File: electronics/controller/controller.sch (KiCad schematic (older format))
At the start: 17 parts

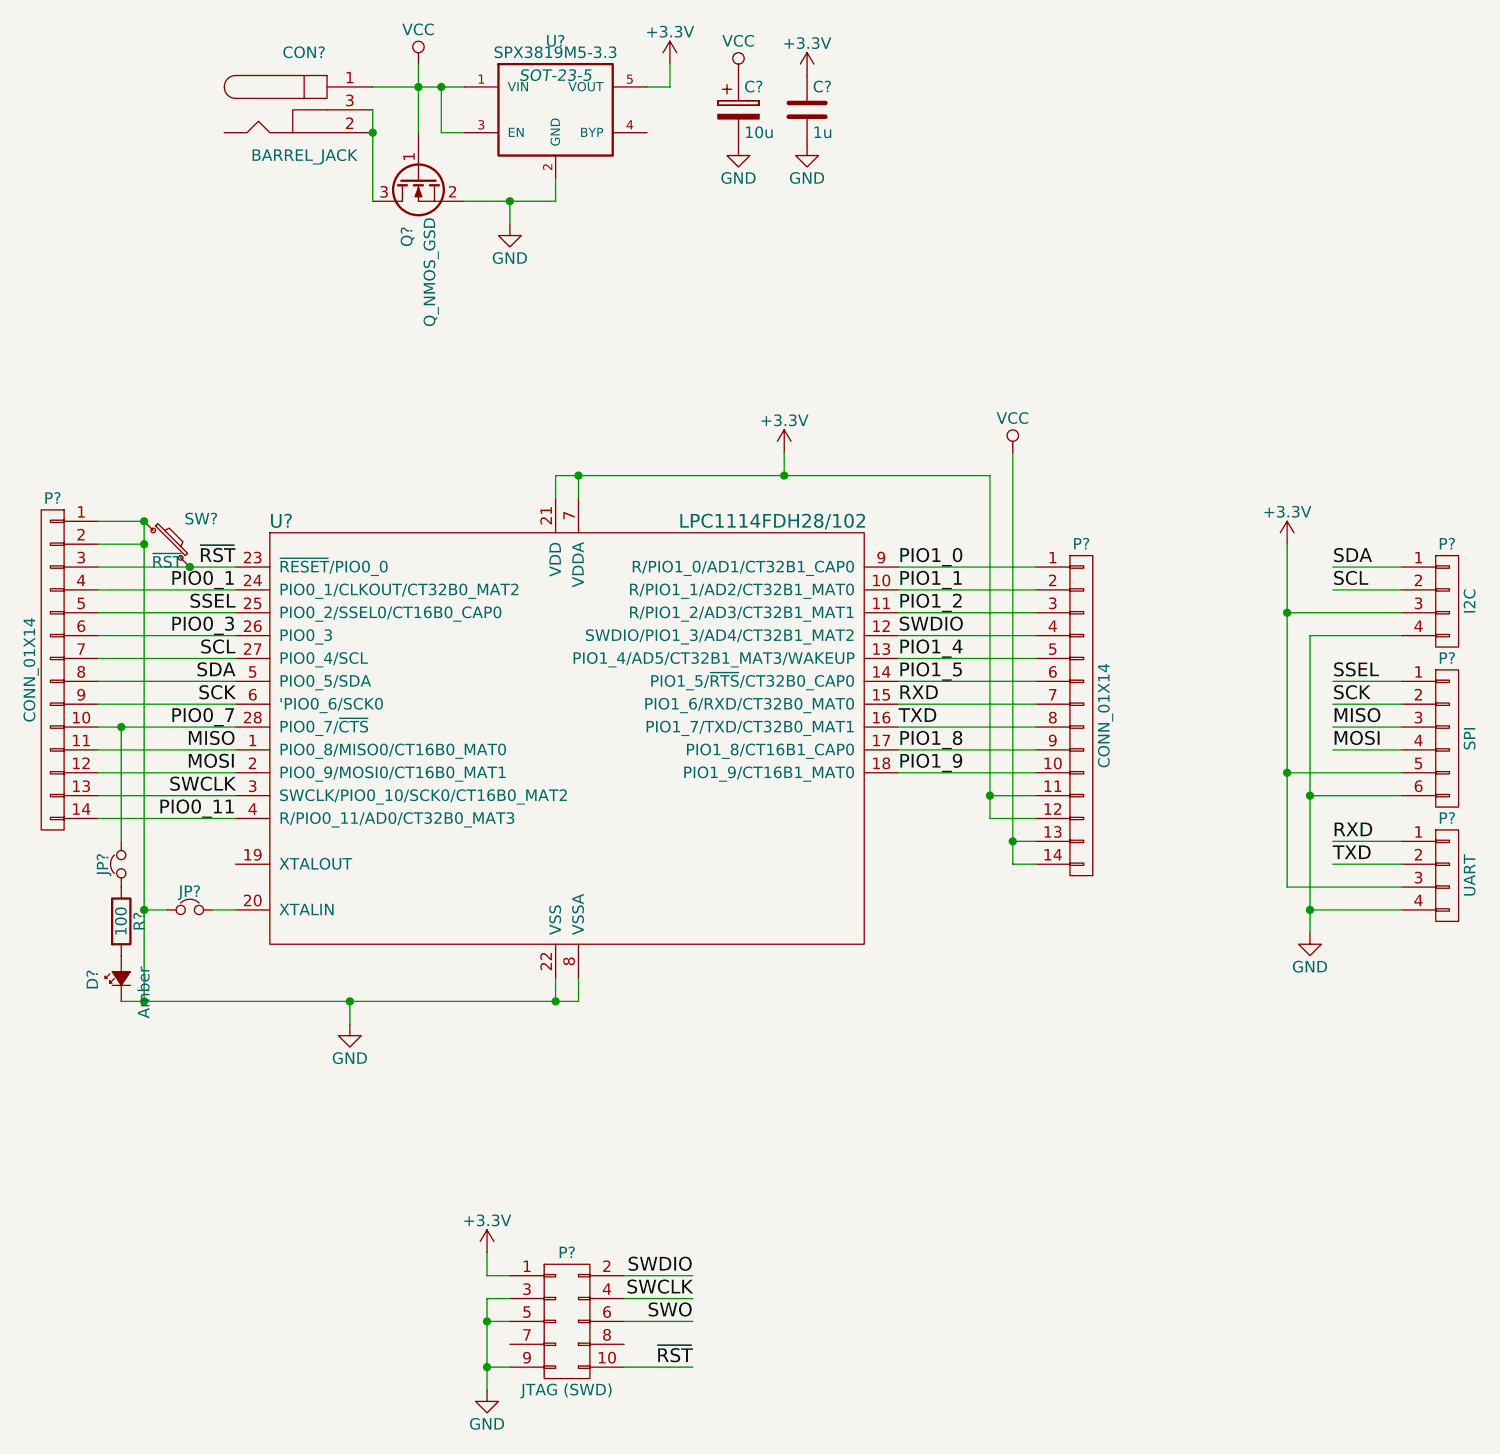
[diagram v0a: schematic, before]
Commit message: Switch to LP2985 regulator, begin board layout
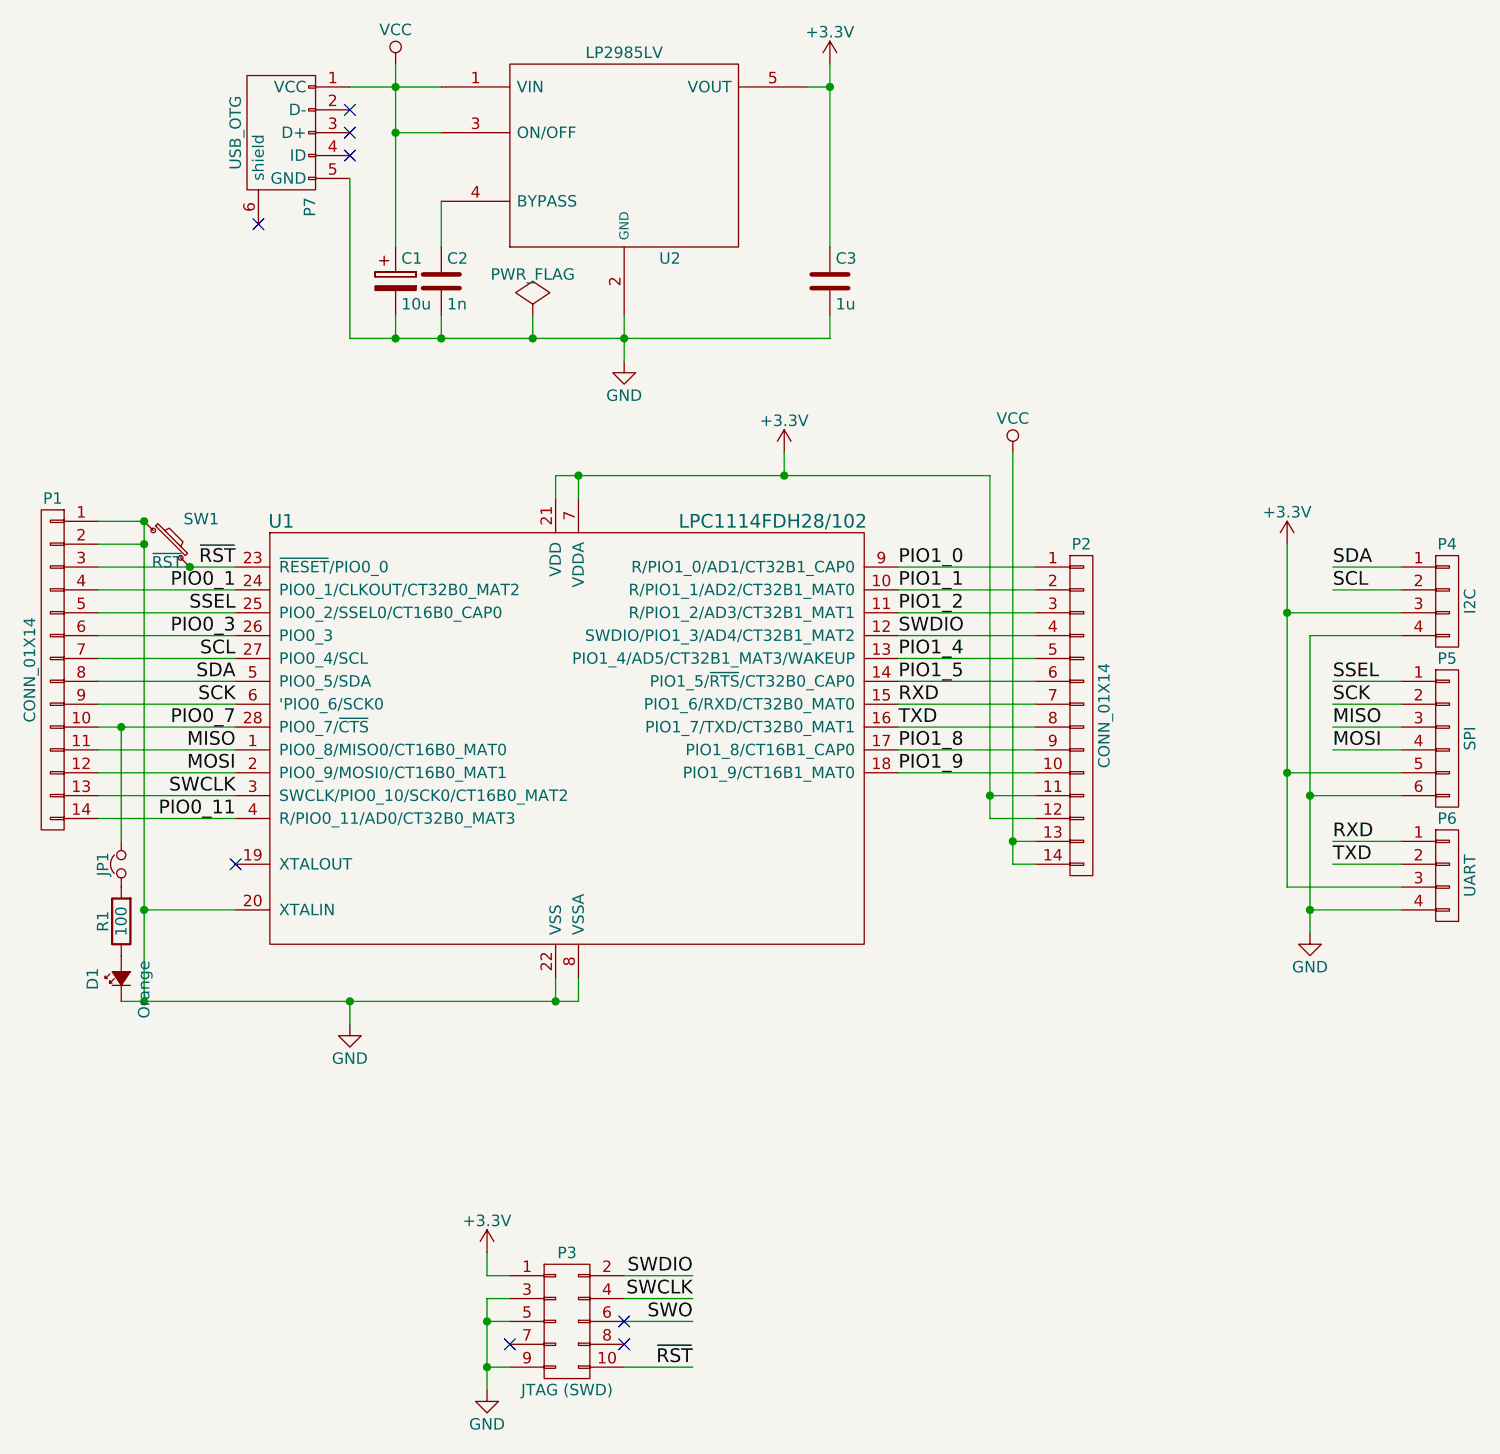
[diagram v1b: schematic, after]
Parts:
- removed CON?: BARREL_JACK, symbol BARREL_JACK
- removed JP?: Jumper_NC_Small, symbol Jumper_NC_Small
- removed Q?: Q_NMOS_GSD, symbol Q_NMOS_GSD
- removed U?: SPX3819M5-3.3, SOT-23-5, symbol SPX3819M5-3.3
- added C2: 1n, Capacitors_SMD:C_0603_HandSoldering, symbol C
- added P7: USB_OTG, Connect:USB_Micro-B, symbol USB_OTG
- added U2: LP2985LV, TO_SOT_Packages_SMD:SOT-23-5, symbol LP2985LV
- C3: renamed from C?; footprint (none) -> Capacitors_SMD:C_0603_HandSoldering
- D1: renamed from D?; value Amber -> Orange; footprint (none) -> LEDs:LED-0603
- P1, P2: renamed from P?; footprint (none) -> Socket_Strips:Socket_Strip_Straight_1x14
- P3: renamed from P?; footprint (none) -> Pin_Headers:Pin_Header_Straight_2x05_Pitch1.27mm
- P4, P6: renamed from P?; footprint (none) -> Connectors_JST_SH:Connectors_JST_BM04B-SRSS-TB
- P5: renamed from P?; footprint (none) -> Connectors_JST_SH:Connectors_JST_BM06B-SRSS-TB
- R1: renamed from R?; footprint (none) -> Resistors_SMD:R_0603_HandSoldering
- U1: renamed from U?; footprint (none) -> Housings_SSOP:TSSOP-28_4.4x9.7mm_Pitch0.65mm
- gave numbers to parts that had none: 3
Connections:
- net +3V3: now also U2.5 (VOUT)
- net GND: now also U1.20 (XTALIN), C2.2, P7.5 (GND), U2.2 (GND)
- net VCC: now also P7.1 (VCC), U2.1 (VIN), U2.3 (ON/OFF)
- net at D1.2 (A): now also R1.1; no longer R1.2
- net at JP1.1: now also R1.2; no longer R1.1
- new net: C2.1, U2.4 (BYPASS)
- no-connect marks 0 -> 8
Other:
- moved on the sheet: C1, C3

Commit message: More work on controller
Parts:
- removed C1: 10u, symbol CP
- added C1: 10u, Capacitors_SMD:C_0805, symbol C
- added C4: 0.1u, Capacitors_SMD:C_0603, symbol C
- C2: footprint Capacitors_SMD:C_0603_HandSoldering -> Capacitors_SMD:C_0603
- C3: value 1u -> 10u; footprint Capacitors_SMD:C_0603_HandSoldering -> Capacitors_SMD:C_0805
- R1: footprint Resistors_SMD:R_0603_HandSoldering -> Resistors_SMD:R_0603
- SW1: footprint (none) -> Buttons_Switches_SMD:SW_SPST_EVQP7A
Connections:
- net +3V3: now also C4.1
- net GND: now also C1.2, C4.2
- net VCC: now also C1.1
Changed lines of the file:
@@
 P 7000 1850
 F 0 "C3" H 7025 1950 50  0000 L CNN
-F 1 "1u" H 7025 1750 50  0000 L CNN
-F 2 "Capacitors_SMD:C_0603_HandSoldering" H 7038 1700 50  0001 C CNN
+F 1 "10u" H 7025 1750 50  0000 L CNN
+F 2 "Capacitors_SMD:C_0805" H 7038 1700 50  0001 C CNN
 F 3 "" H 7000 1850 50  0000 C CNN
 	1    7000 1850
-	1    0    0    -1
-$EndComp
-$Comp
-L CP C1
-U 1 1 57098845
-P 5100 1850
-F 0 "C1" H 5125 1950 50  0000 L CNN
-F 1 "10u" H 5125 1750 50  0000 L CNN
-F 2 "" H 5138 1700 50  0001 C CNN
-F 3 "" H 5100 1850 50  0000 C CNN
-	1    5100 1850
 	1    0    0    -1
 $EndComp
@@
 F 0 "SW1" H 4250 3110 50  0000 C CNN
 F 1 "~RST~" H 4100 2921 50  0000 C CNN
-F 2 "" H 4100 3000 50  0001 C CNN
+F 2 "Buttons_Switches_SMD:SW_SPST_EVQP7A" H 4100 3000 50  0001 C CNN
 F 3 "" H 4100 3000 50  0000 C CNN
 	1    4100 3000
@@
 F 0 "R1" V 3980 4650 50  0000 C CNN
 F 1 "100" V 3900 4650 50  0000 C CNN
-F 2 "Resistors_SMD:R_0603_HandSoldering" V 3830 4650 50  0001 C CNN
+F 2 "Resistors_SMD:R_0603" V 3830 4650 50  0001 C CNN
 F 3 "" H 3900 4650 50  0000 C CNN
 	1    3900 4650
@@
 F 0 "C2" H 5325 1950 50  0000 L CNN
 F 1 "1n" H 5325 1750 50  0000 L CNN
-F 2 "Capacitors_SMD:C_0603_HandSoldering" H 5338 1700 50  0001 C CNN
+F 2 "Capacitors_SMD:C_0603" H 5338 1700 50  0001 C CNN
 F 3 "" H 5300 1850 50  0000 C CNN
 	1    5300 1850
@@
 	5700 2100 5700 2000
 Connection ~ 5700 2100
+$Comp
+L C C1
+U 1 1 5716C093
+P 5100 1850
+F 0 "C1" H 5125 1950 50  0000 L CNN
+F 1 "10u" H 5125 1750 50  0000 L CNN
+F 2 "Capacitors_SMD:C_0805" H 5138 1700 50  0001 C CNN
+F 3 "" H 5100 1850 50  0000 C CNN
+	1    5100 1850
+	1    0    0    -1
+$EndComp
+$Comp
+L C C4
+U 1 1 5716C2B2
+P 7400 4550
+F 0 "C4" H 7425 4650 50  0000 L CNN
+F 1 "0.1u" H 7425 4450 50  0000 L CNN
+F 2 "Capacitors_SMD:C_0603" H 7438 4400 50  0001 C CNN
+F 3 "" H 7400 4550 50  0000 C CNN
+	1    7400 4550
+	1    0    0    -1
+$EndComp
+$Comp
+L +3.3V #PWR012
+U 1 1 5716C3C3
+P 7400 4400
+F 0 "#PWR012" H 7400 4250 50  0001 C CNN
+F 1 "+3.3V" H 7400 4540 50  0000 C CNN
+F 2 "" H 7400 4400 50  0000 C CNN
+F 3 "" H 7400 4400 50  0000 C CNN
+	1    7400 4400
+	1    0    0    -1
+$EndComp
+$Comp
+L GND #PWR013
+U 1 1 5716C401
+P 7400 4700
+F 0 "#PWR013" H 7400 4450 50  0001 C CNN
+F 1 "GND" H 7400 4550 50  0000 C CNN
+F 2 "" H 7400 4700 50  0000 C CNN
+F 3 "" H 7400 4700 50  0000 C CNN
+	1    7400 4700
+	1    0    0    -1
+$EndComp
 $EndSCHEMATC
